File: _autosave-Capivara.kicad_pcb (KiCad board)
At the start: 2 copper layers, 52 x 49 mm, 62 parts, among them J1 COMM, J2 PROG, J3 INSTR, J4 GENERAL, J5 UART, J6 DAC_OUT, U1 STM32F303CCTx, U2 AMS1117-3.3, U3 REF3012, U4 MCP6002-xSN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

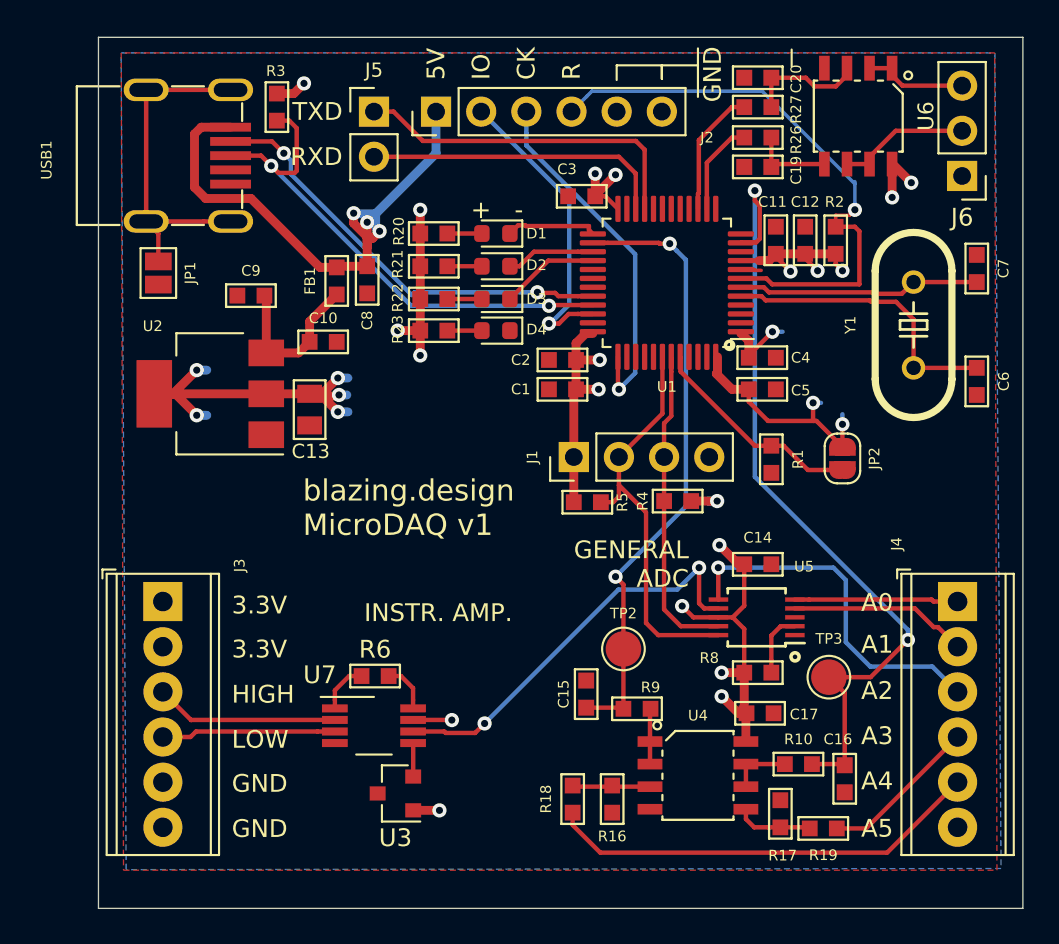
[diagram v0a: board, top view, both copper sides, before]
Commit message: Usar INA ao invés de InsOp discreto
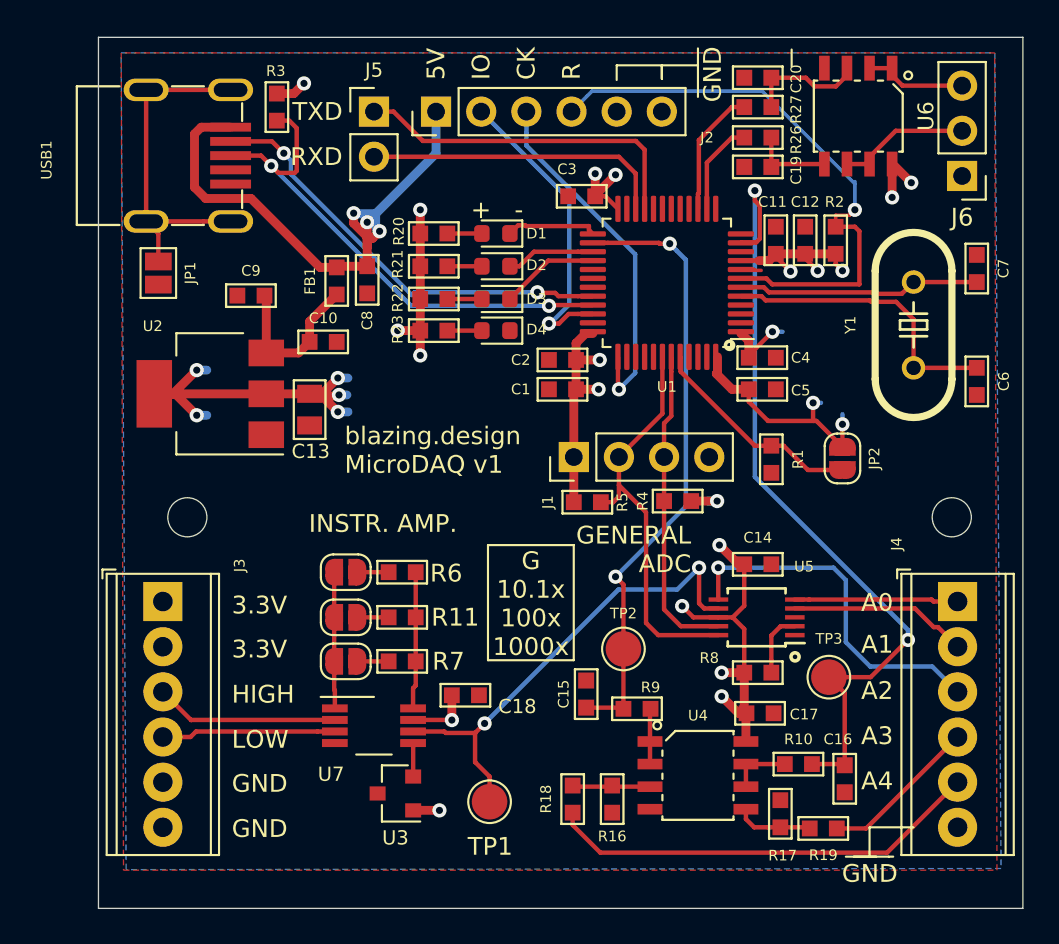
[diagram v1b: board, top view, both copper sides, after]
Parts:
- added C18: 100nF, OPL_Resistor:R0603, F.Cu at (48.6, 80.0)
- added JP3: 1000x, Jumper:SolderJumper-2_P1.3mm_Open_RoundedPad1.0x1.5mm, F.Cu at (41.9, 78.1)
- added JP4: 100x, Jumper:SolderJumper-2_P1.3mm_Open_RoundedPad1.0x1.5mm, F.Cu at (41.9, 75.6)
- added JP5: 10x, Jumper:SolderJumper-2_P1.3mm_Open_RoundedPad1.0x1.5mm, F.Cu at (41.9, 73.1)
- added R11: 1k, OPL_Resistor:R0603, F.Cu at (45.1, 75.6)
- added R7: 100, OPL_Resistor:R0603, F.Cu at (45.1, 78.1)
- added REF**: MountingHole_2.2mm_M2, MountingHole:MountingHole_2.2mm_M2, F.Cu at (76.0, 70.0)
- added REF**: MountingHole_2.2mm_M2, MountingHole:MountingHole_2.2mm_M2, F.Cu at (33.0, 70.0)
- added TP1: IN_AMP, TestPoint:TestPoint_Pad_D2.0mm, F.Cu at (50.0, 86.0)
- R6: value 1k -> 10k
- moved R6 6.04 mm to (45.1, 73.1)
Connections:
- R6 pad 1: Net-(R6-Pad1) -> Net-(JP5-Pad2)
- U7 pad 1: Net-(R6-Pad1) -> Net-(JP3-Pad1)
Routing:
- net Net-(JP3-Pad1): track 0.00 -> 7.68 mm
- net Net-(R11-Pad2): track 2.80 -> 7.72 mm
- net A3: track 23.2 -> 27.4 mm
- net Net-(R6-Pad1): track 2.85 -> 0.00 mm
- net Net-(JP5-Pad2): track 0.00 -> 1.76 mm
- net Net-(JP4-Pad2): track 0.00 -> 1.76 mm
- net Net-(JP3-Pad2): track 0.00 -> 1.76 mm
- net +3.3VADC: track 106.0 -> 107.3 mm
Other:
- board text added: "G 10.1x 100x 1000x"
- board text removed: "A5"
